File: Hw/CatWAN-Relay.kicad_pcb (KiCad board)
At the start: 2 copper layers, 50 x 86.9 mm, 55 parts, among them J2 INPUTS, J3 OUTPUTS, J4 I2C, J5 Serial, P1 USB_C_Plug_USB2.0, Q1 MMBT2222A, Q2 MMBT2222A, Q3 MMBT2222A, SW1 BOOT, SW2 RESET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

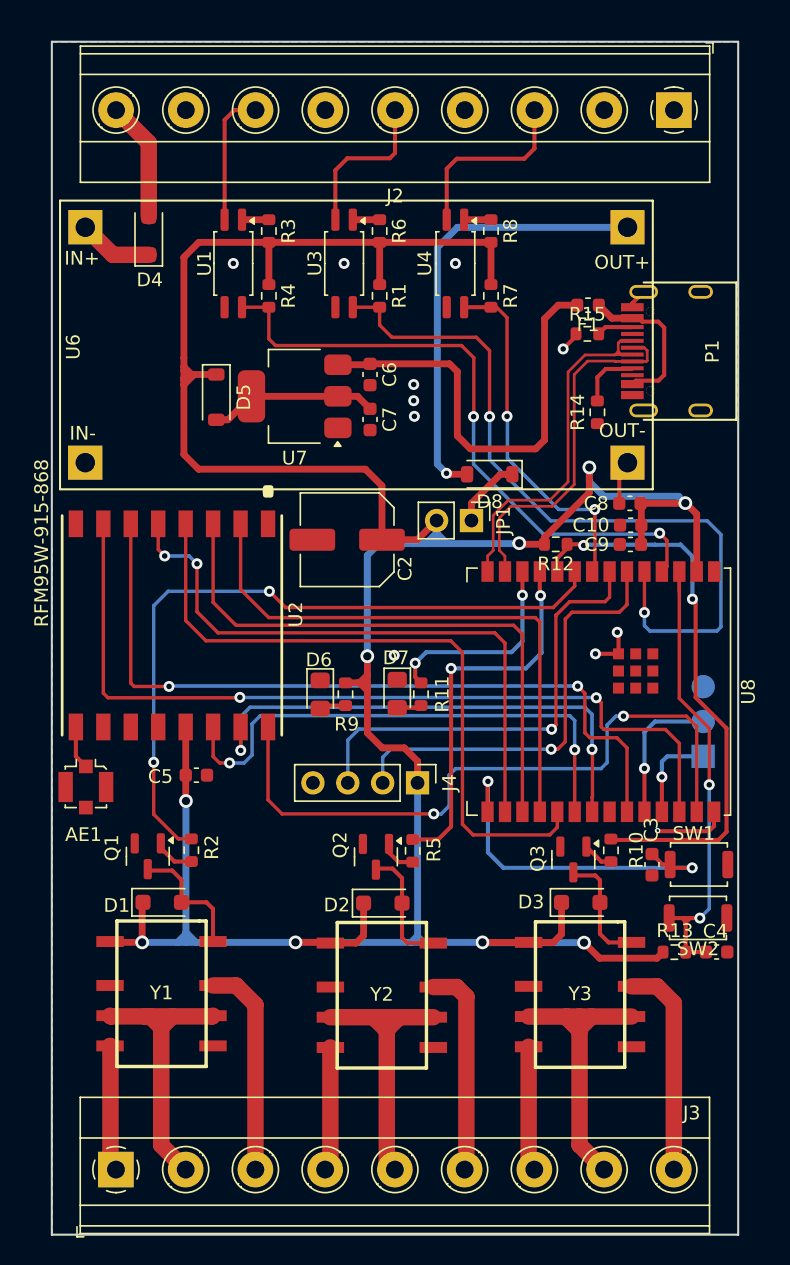
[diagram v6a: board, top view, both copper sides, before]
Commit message: feat: change routes width
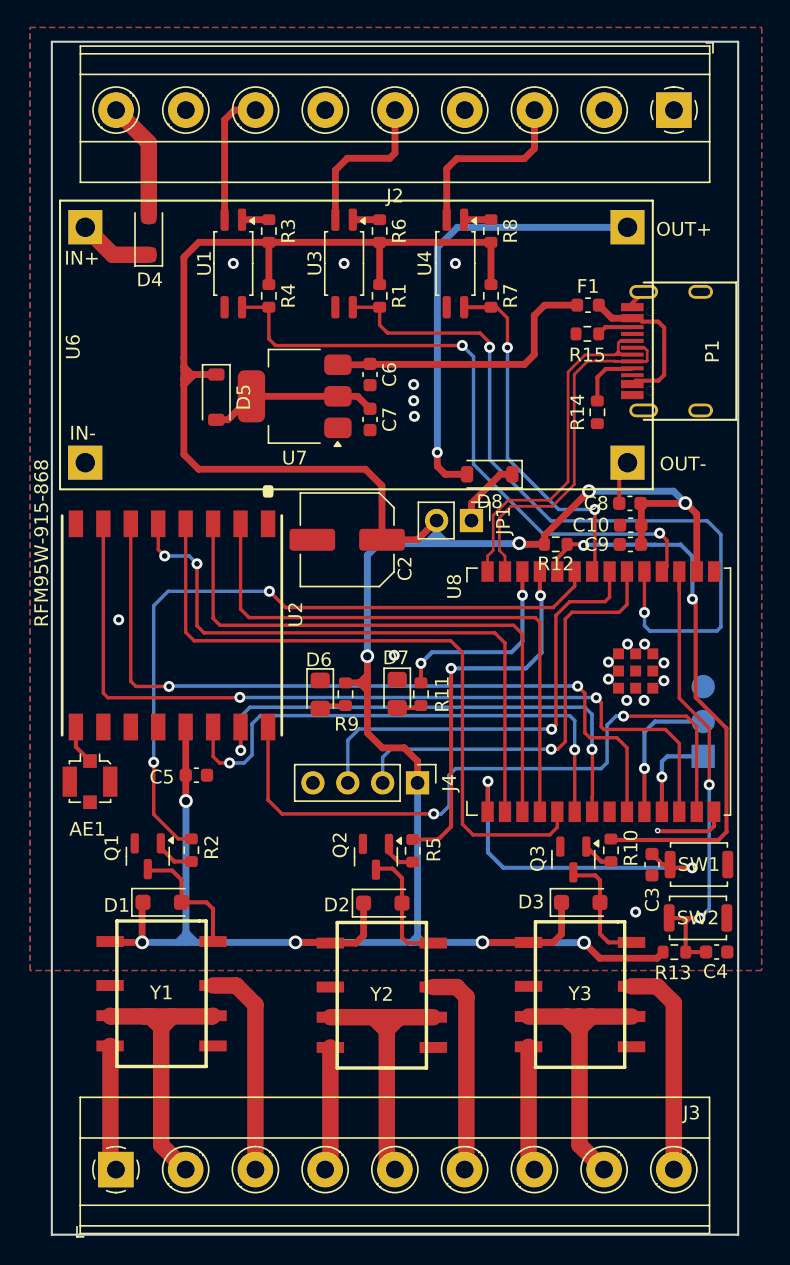
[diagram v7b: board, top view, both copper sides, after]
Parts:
- moved AE1 0.49 mm to (44.2, 91.5)
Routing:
- net VBUS: track 32.3 -> 20.9 mm
- net GND: track 14.8 -> 10.0 mm, vias 11 -> 18
- net +3V3: track 233.0 -> 229.9 mm
- net /MISO: track 41.4 -> 42.2 mm
- net /MOSI: track 42.2 -> 42.8 mm
- net /RX_LED: track 15.2 -> 14.6 mm
- net /SS: track 44.4 -> 45.0 mm
- net /SCK: track 49.3 -> 49.8 mm

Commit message: fix: move labels
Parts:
- moved D8 3.11 mm to (70.4, 68.3)
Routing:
- net Net-(D8-A): track 32.8 -> 31.3 mm
- net Net-(D8-K): track 5.11 -> 4.19 mm
- net GND: vias 18 -> 49
